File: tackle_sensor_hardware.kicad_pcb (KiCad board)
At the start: 2 copper layers, 50.8 x 50.8 mm, 39 parts, among them J1 Conn_01x02_Male, J2 Conn_01x04_Male, J3 Conn_01x02_Male, J4 Conn_ARM_JTAG_SWD_10, Q1 DMP4051LK3, Q2 2N7002K, Q3 2N7002K, Q4 2N7002K, Q5 2N7002K, Q6 2N7002K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

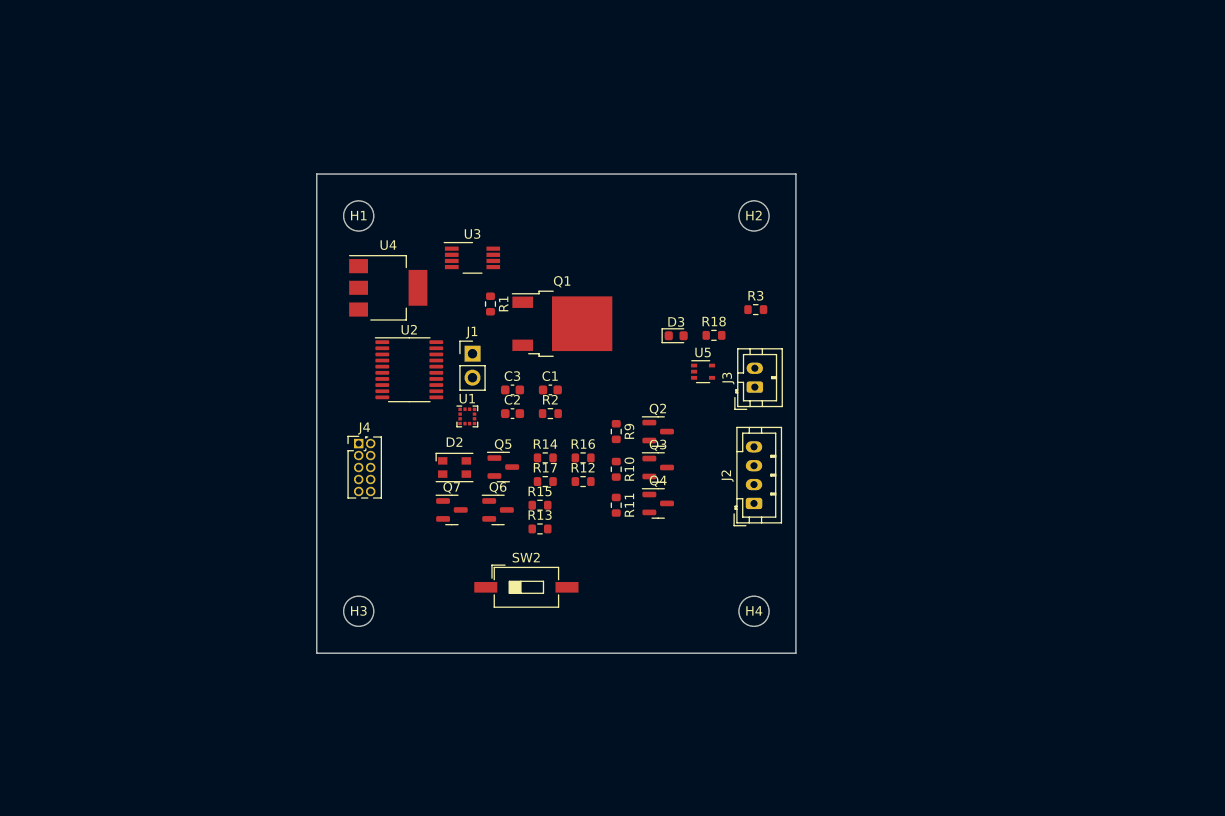
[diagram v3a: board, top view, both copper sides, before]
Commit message: updated connectors, added 0 ohm resistors
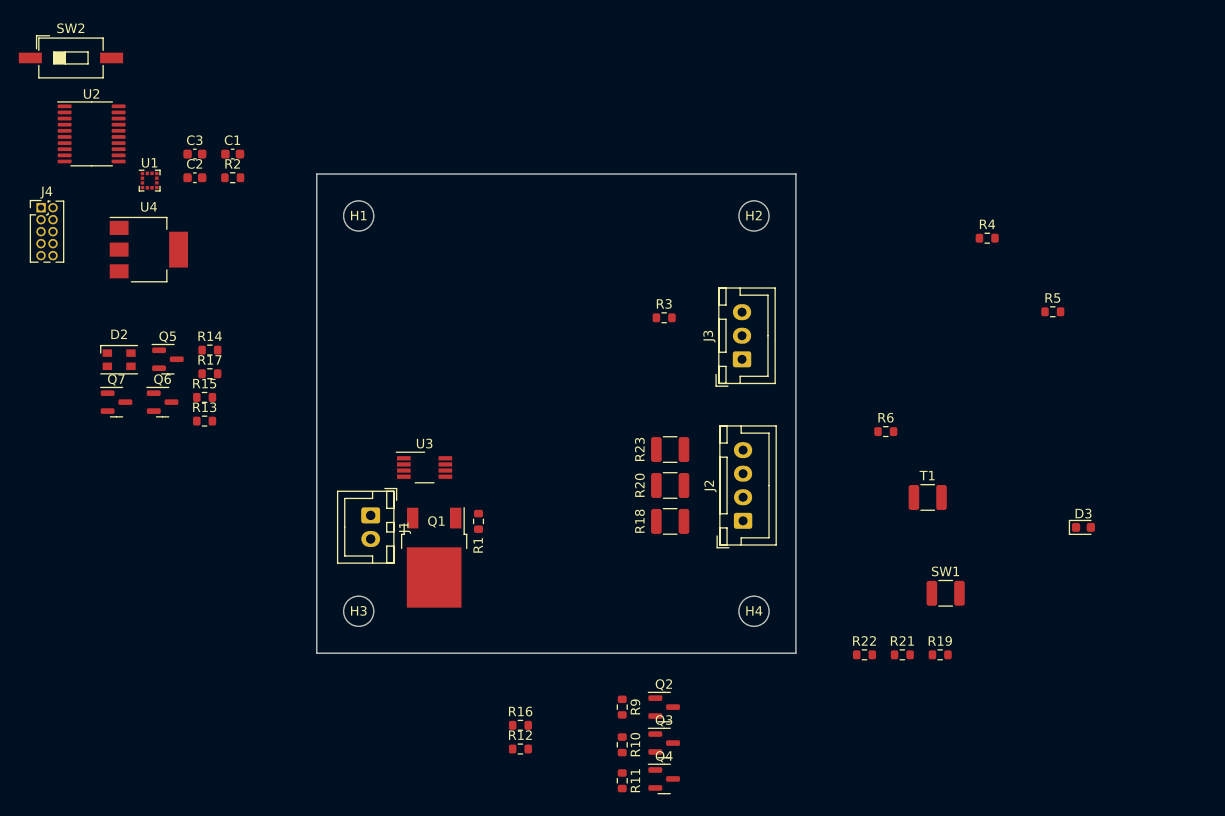
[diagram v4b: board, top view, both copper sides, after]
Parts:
- removed U5: 74LVC1G17, Package_TO_SOT_SMD:SOT-353_SC-70-5
- added R19: 1k, Resistor_SMD:R_0603_1608Metric, F.Cu at (186.7, 120.8)
- added R20: 0, Resistor_SMD:R_1210_3225Metric, F.Cu at (158.1, 102.9)
- added R21: 150, Resistor_SMD:R_0603_1608Metric, F.Cu at (182.7, 120.8)
- added R22: 150, Resistor_SMD:R_0603_1608Metric, F.Cu at (178.7, 120.8)
- added R23: 0, Resistor_SMD:R_1210_3225Metric, F.Cu at (158.1, 99.1)
- added R4: R_US, Resistor_SMD:R_0603_1608Metric, F.Cu at (191.7, 76.7)
- added R5: R_US, Resistor_SMD:R_0603_1608Metric, F.Cu at (198.7, 84.5)
- added R6: 25m, Resistor_SMD:R_0603_1608Metric, F.Cu at (181.0, 97.2)
- added SW1: SW_Push, Resistor_SMD:R_1210_3225Metric, F.Cu at (187.3, 114.3)
- added T1: DRQ125-330-R, Resistor_SMD:R_1210_3225Metric, F.Cu at (185.4, 104.1)
- J1: footprint Connector_PinHeader_2.54mm:PinHeader_1x02_P2.54mm_Vertical -> Connector_JST:JST_XH_B2B-XH-A_1x02_P2.50mm_Vertical
- J2: footprint Connector_JST:JST_PH_B4B-PH-K_1x04_P2.00mm_Vertical -> Connector_JST:JST_XH_B4B-XH-A_1x04_P2.50mm_Vertical
- J3: value Conn_01x02_Male -> Conn_01x03_Male; footprint Connector_JST:JST_PH_B2B-PH-K_1x02_P2.00mm_Vertical -> Connector_JST:JST_XH_B3B-XH-A_1x03_P2.50mm_Vertical
- R18: value 1k -> 0; footprint Resistor_SMD:R_0603_1608Metric -> Resistor_SMD:R_1210_3225Metric
- moved SW2 74.0 mm to (94.6, 57.5)
- moved D3 47.7 mm to (201.9, 107.3)
- moved C2 41.9 mm to (107.7, 70.2)
- moved C3 41.9 mm to (107.7, 67.7)
- moved U1 41.9 mm to (102.9, 70.5)
- moved U2 41.9 mm to (96.8, 65.6)
- moved C1 41.9 mm to (111.7, 67.7)
- moved J4 41.9 mm to (91.4, 73.4)
- moved R2 41.9 mm to (111.7, 70.2)
- moved Q5 37.4 mm to (104.9, 89.5)
- moved D2 37.4 mm to (99.7, 89.5)
- moved Q6 37.4 mm to (104.3, 94.0)
- moved R13 37.4 mm to (108.8, 96.0)
- moved R14 37.4 mm to (109.3, 88.5)
- moved R15 37.4 mm to (108.8, 93.5)
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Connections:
- D3 pad 2: TACKLE_STATUS -> +3V3
- J3 pad 2: GND -> Net-(J3-Pad2)
- Q2 pad 3: Net-(J2-Pad2) -> Net-(Q2-Pad3)
- Q3 pad 3: Net-(J2-Pad3) -> Net-(Q3-Pad3)
- Q4 pad 3: Net-(J2-Pad4) -> Net-(Q4-Pad3)
- R18 pad 1: Net-(D3-Pad1) -> Net-(Q2-Pad3)
- R18 pad 2: GND -> Net-(J2-Pad2)

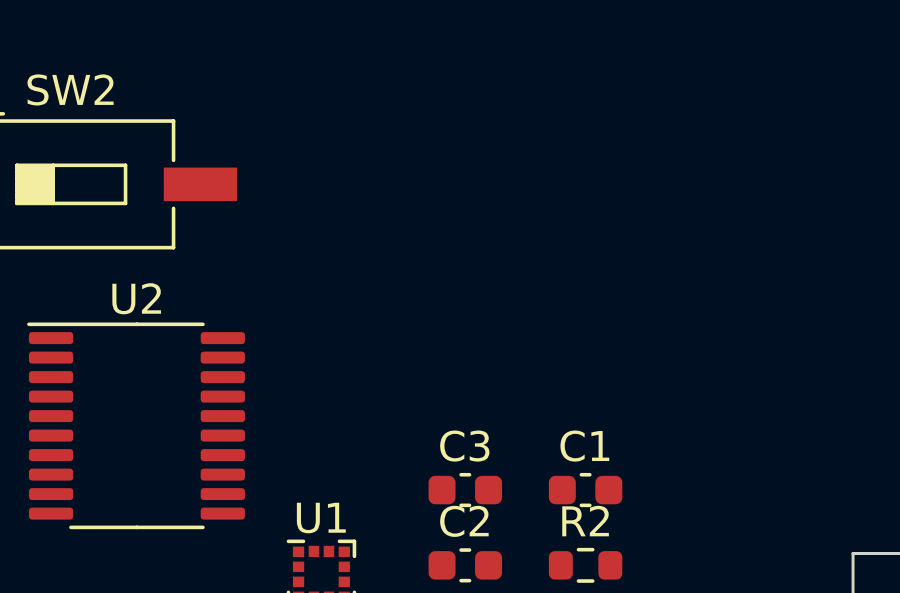
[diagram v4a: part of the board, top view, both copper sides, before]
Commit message: added pinout to MCU
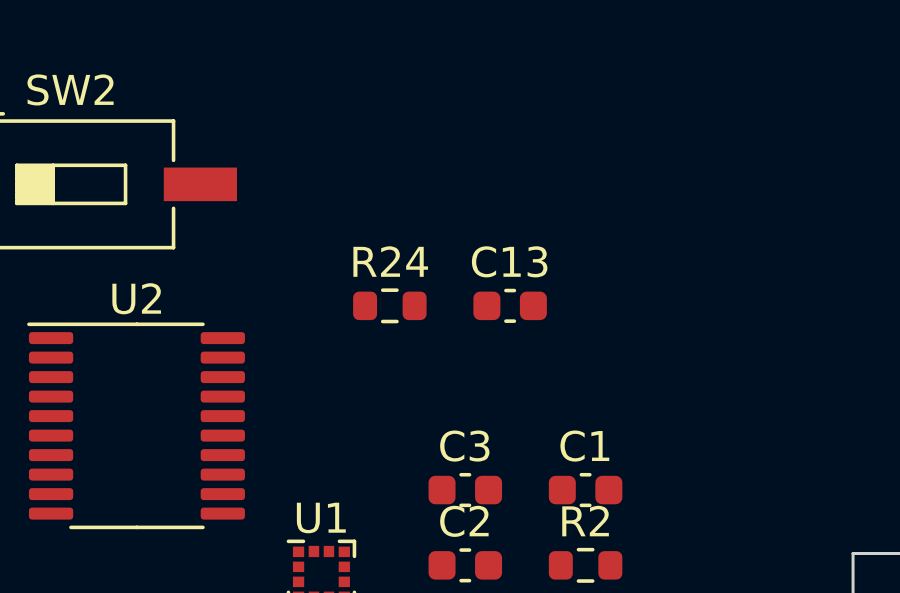
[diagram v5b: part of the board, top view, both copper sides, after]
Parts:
- added C13: 100n, Capacitor_SMD:C_0603_1608Metric, F.Cu at (109.2, 61.6)
- added R24: 10k, Resistor_SMD:R_0603_1608Metric, F.Cu at (105.2, 61.6)
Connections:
- SW2 pad 1: unconnected-(SW2-Pad1) -> Net-(U2-Pad3)
- SW2 pad 2: unconnected-(SW2-Pad2) -> GND
- U1 pad 1: unconnected-(U1-Pad1) -> /SPI1_SCK
- U1 pad 11: unconnected-(U1-Pad11) -> /ACC_INT2
- U1 pad 12: unconnected-(U1-Pad12) -> /ACC_INT1
- U1 pad 2: unconnected-(U1-Pad2) -> /SPI1_NSS
- U1 pad 3: unconnected-(U1-Pad3) -> /SPI1_MISO
- U1 pad 4: unconnected-(U1-Pad4) -> /SPI1_MOSI
- U2 pad 10: unconnected-(U2-Pad10) -> UART_RX
- U2 pad 11: unconnected-(U2-Pad11) -> /SPI1_NSS
- U2 pad 12: unconnected-(U2-Pad12) -> /ACC_INT2
- U2 pad 13: unconnected-(U2-Pad13) -> /SPI1_MISO
- U2 pad 14: unconnected-(U2-Pad14) -> /SPI1_MOSI
- U2 pad 15: unconnected-(U2-Pad15) -> B_PWM
- U2 pad 16: unconnected-(U2-Pad16) -> G_PWM
- U2 pad 2: unconnected-(U2-Pad2) -> TACKLE_STATUS
- U2 pad 20: unconnected-(U2-Pad20) -> R_PWM
- U2 pad 3: unconnected-(U2-Pad3) -> Net-(U2-Pad3)
- U2 pad 7: unconnected-(U2-Pad7) -> /ACC_INT1
- U2 pad 8: unconnected-(U2-Pad8) -> /SPI1_SCK
- U2 pad 9: unconnected-(U2-Pad9) -> UART_TX
- U4 pad 1: Net-(C11-Pad2) -> GND

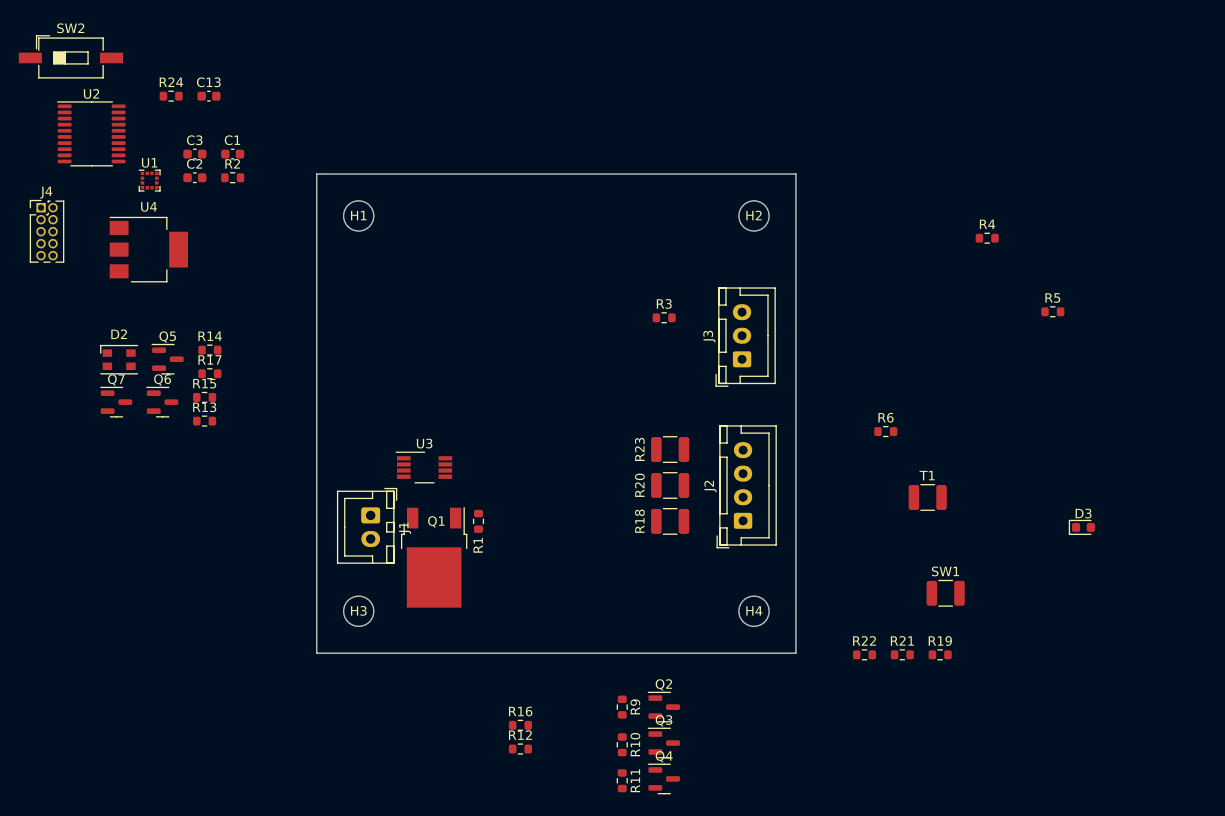
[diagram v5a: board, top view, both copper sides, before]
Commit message: added eFuse, added mosfet, added footprints
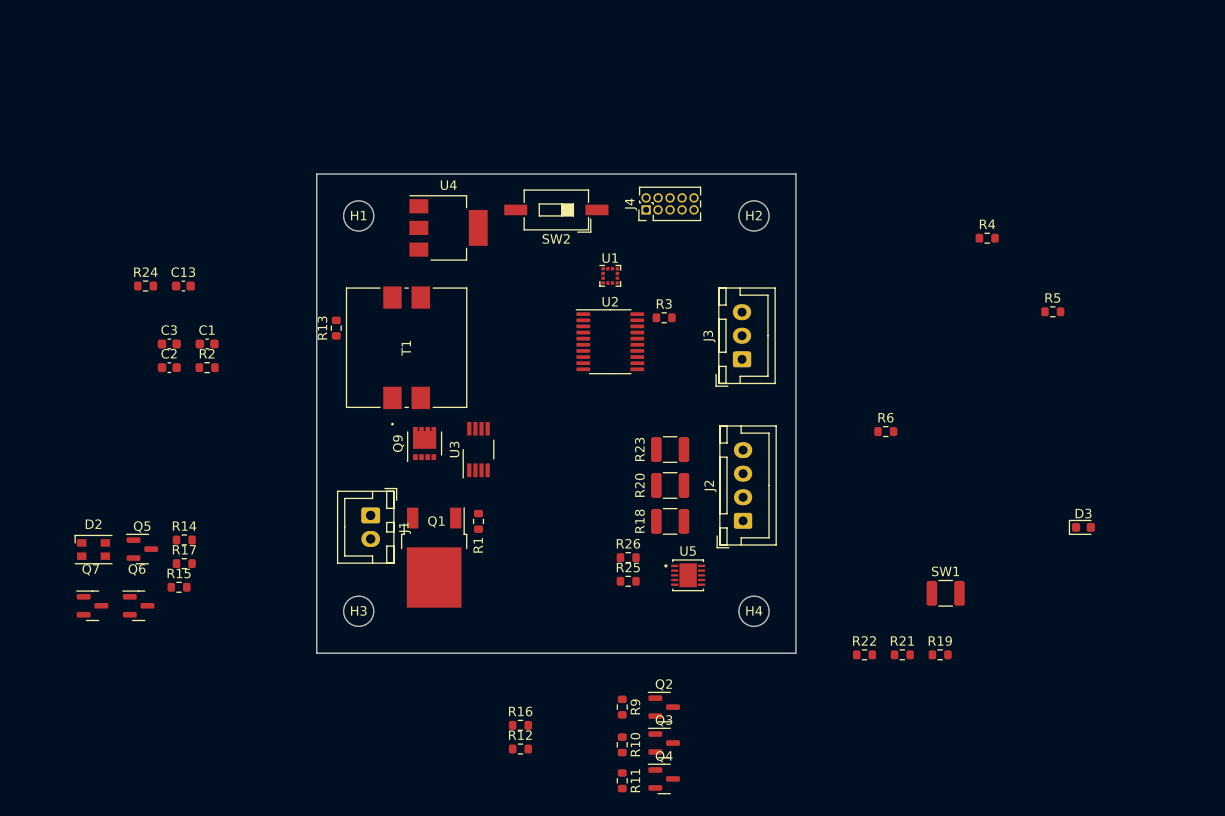
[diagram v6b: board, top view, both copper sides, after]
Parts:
- added Q9: CSD19538Q3A, Package_SON:VSON-8_3.3x3.3mm_P0.65mm_NexFET, F.Cu at (132.1, 98.4)
- added R25: 1k, Resistor_SMD:R_0603_1608Metric, F.Cu at (153.7, 113.0)
- added R26: 1k, Resistor_SMD:R_0603_1608Metric, F.Cu at (153.7, 110.5)
- added U5: NIS5420MT6TXG, rfc_footprint_lib:WDFN10_522AA-01_ONS, F.Cu at (160.0, 112.4)
- T1: footprint Resistor_SMD:R_1210_3225Metric -> rfc_footprint_lib:DRQ125-150-R
- moved J4 64.2 mm to (155.6, 73.7), turned to 90 degrees
- moved U2 59.2 mm to (151.8, 87.6)
- moved T1 57.5 mm to (130.2, 88.3), turned to 90 degrees
- moved SW2 53.9 mm to (146.1, 73.7), turned to 180 degrees
- moved U1 49.9 mm to (151.8, 80.6)
- moved U4 31.9 mm to (134.6, 75.6)
- moved Q6 21.7 mm to (101.8, 115.6)
- moved Q7 21.7 mm to (96.9, 115.6)
- moved D2 20.3 mm to (97.0, 109.7)
- moved R15 20.3 mm to (106.0, 113.7)
- moved C1 20.3 mm to (109.0, 87.9)
- moved C13 20.3 mm to (106.5, 81.7)
- moved C2 20.3 mm to (105.0, 90.4)
- moved C3 20.3 mm to (105.0, 87.9)
- moved Q5 20.3 mm to (102.2, 109.6)
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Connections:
- J2 pad 1: +12V -> Net-(J2-Pad1)
- U2 pad 1: unconnected-(U2-Pad1) -> EN_FAULT_EFUSE
- U3 pad 6: unconnected-(U3-Pad6) -> Net-(U3-Pad6)

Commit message: Picked most RC components and footprints
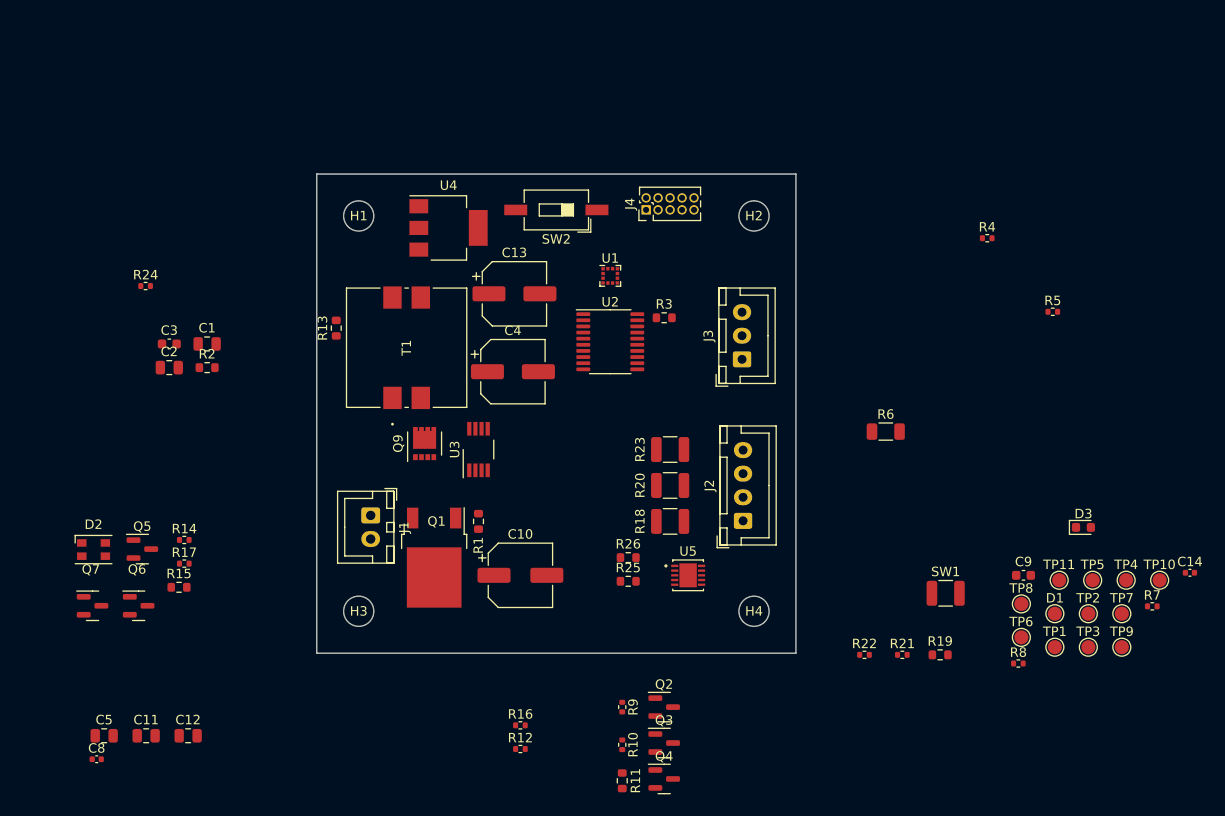
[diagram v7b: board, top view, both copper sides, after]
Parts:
- added C10: 22uF, 20V, Capacitor_SMD:CP_Elec_6.3x5.9, F.Cu at (142.2, 112.4)
- added C11: 100nF, 50V, Capacitor_SMD:C_0805_2012Metric, F.Cu at (102.6, 129.4)
- added C12: 100nF, 50V, Capacitor_SMD:C_0805_2012Metric, F.Cu at (107.0, 129.4)
- added C14: DNP, Capacitor_SMD:C_0402_1005Metric, F.Cu at (213.2, 112.1)
- added C4: 10uF, 50V, Capacitor_SMD:CP_Elec_6.3x5.8, F.Cu at (141.4, 90.8)
- added C5: 100nF, 50V, Capacitor_SMD:C_0805_2012Metric, F.Cu at (98.1, 129.4)
- added C8: 1nF, 50V, Capacitor_SMD:C_0402_1005Metric, F.Cu at (97.3, 131.9)
- added C9: 1uF, 50V, Capacitor_SMD:C_0603_1608Metric, F.Cu at (195.6, 112.4)
- added D1: SS2PH10HM3_A/H, TestPoint:TestPoint_Pad_D1.5mm, F.Cu at (198.9, 116.5)
- added R7: 84.5k,1%,63mW, Resistor_SMD:R_0402_1005Metric, F.Cu at (209.2, 115.7)
- added R8: 10k,1%,63mW, Resistor_SMD:R_0402_1005Metric, F.Cu at (195.0, 121.7)
- added TP1: TestPoint, TestPoint:TestPoint_Pad_D1.5mm, F.Cu at (198.9, 120.0)
- added TP10: TestPoint, TestPoint:TestPoint_Pad_D1.5mm, F.Cu at (210.0, 112.9)
- added TP11: TestPoint, TestPoint:TestPoint_Pad_D1.5mm, F.Cu at (199.4, 112.9)
- added TP2: TestPoint, TestPoint:TestPoint_Pad_D1.5mm, F.Cu at (202.4, 116.5)
- added TP3: TestPoint, TestPoint:TestPoint_Pad_D1.5mm, F.Cu at (202.4, 120.0)
- added TP4: TestPoint, TestPoint:TestPoint_Pad_D1.5mm, F.Cu at (206.5, 112.9)
- added TP5: TestPoint, TestPoint:TestPoint_Pad_D1.5mm, F.Cu at (202.9, 112.9)
- added TP6: TestPoint, TestPoint:TestPoint_Pad_D1.5mm, F.Cu at (195.3, 119.0)
- added TP7: TestPoint, TestPoint:TestPoint_Pad_D1.5mm, F.Cu at (206.0, 116.5)
- added TP8: TestPoint, TestPoint:TestPoint_Pad_D1.5mm, F.Cu at (195.3, 115.4)
- added TP9: TestPoint, TestPoint:TestPoint_Pad_D1.5mm, F.Cu at (206.0, 120.0)
- C1, C2: value 100n -> 100nF, 50V; footprint Capacitor_SMD:C_0603_1608Metric -> Capacitor_SMD:C_0805_2012Metric
- C13: value 100n -> 10uF, 50V; footprint Capacitor_SMD:C_0603_1608Metric -> Capacitor_SMD:CP_Elec_6.3x5.8
- R1, R13, R15, R19: value 1k -> 1k,1%,25mW
- R10, R12, R14, R16, R24, R9: value 10k -> 10k,1%,63mW; footprint Resistor_SMD:R_0603_1608Metric -> Resistor_SMD:R_0402_1005Metric
- R11: value 10k -> 1k,1%,25mW
- R17: value 1k -> 10k,1%,63mW; footprint Resistor_SMD:R_0603_1608Metric -> Resistor_SMD:R_0402_1005Metric
- R21, R22: value 150 -> 220,1%,63mW; footprint Resistor_SMD:R_0603_1608Metric -> Resistor_SMD:R_0402_1005Metric
- R4: value R_US -> 56.2k,1%,63mW; footprint Resistor_SMD:R_0603_1608Metric -> Resistor_SMD:R_0402_1005Metric
- R5: value R_US -> 100,1%,63mW; footprint Resistor_SMD:R_0603_1608Metric -> Resistor_SMD:R_0402_1005Metric
- R6: value 25m -> 25mOhm,1%,500mW; footprint Resistor_SMD:R_0603_1608Metric -> Resistor_SMD:R_1206_3216Metric
- moved C13 35.1 mm to (141.6, 82.5)
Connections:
- C1 pad 1: +3V3 -> /RST
- C13 pad 1: /RST -> +3V3
- R10 pad 1: G_PWM -> R_PWM
- R11 pad 1: B_PWM -> Net-(D2-Pad1)
- R11 pad 2: GND -> Net-(Q5-Pad3)
- R12 pad 1: R_PWM -> G_PWM
- R13 pad 1: Net-(D2-Pad1) -> Net-(D2-Pad4)
- R13 pad 2: Net-(Q5-Pad3) -> Net-(Q6-Pad3)
- R14 pad 1: G_PWM -> B_PWM
- R15 pad 1: Net-(D2-Pad4) -> Net-(D2-Pad3)
- R15 pad 2: Net-(Q6-Pad3) -> Net-(Q7-Pad3)
- R16 pad 1: B_PWM -> R_PWM
- R17 pad 1: Net-(D2-Pad3) -> G_PWM
- R17 pad 2: Net-(Q7-Pad3) -> GND
- R24 pad 1: +3V3 -> B_PWM
- R24 pad 2: Net-(R24-Pad2) -> GND
- R9 pad 1: R_PWM -> +3V3
- R9 pad 2: GND -> Net-(SW2-Pad1)
- SW2 pad 1: Net-(R24-Pad2) -> Net-(SW2-Pad1)
- U2 pad 3: Net-(R24-Pad2) -> Net-(SW2-Pad1)

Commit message: add graphic
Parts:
- added G***: LOGO, rfc_footprint_lib:logo_inv, B.Cu at (146.1, 91.4)
- moved C4 1.27 mm to (141.4, 89.5)
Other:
- board text added: "Robotic Football Tackle Sensor V0.0 4/15/2022"
